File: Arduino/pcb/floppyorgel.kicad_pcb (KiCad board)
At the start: 2 copper layers, 50 x 50 mm, 13 parts, among them J1 Floppy-Bus, J2 Floppy-Bus, J3 FTDI, J4 Buck Converter 5V, J5 MAX485 Socket, J6 Buck Converter 12V, J7 IBM_PC_IDC_Connector, J8 Power Select, J9 Floppy Power, SW1 Bus Address Select, SW2 Reset Button, U1 ATMEGA328P-AU

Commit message: pcb: update
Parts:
- removed REF**: Floppy_Power, Pin_Headers:Pin_Header_Straight_1x04_Pitch2.54mm
- added U2: 74HC595, SMD_Packages:SO-16-N, F.Cu at (108.0, 113.0)
- added U3: 74LS166, SMD_Packages:SO-16-N, F.Cu at (142.0, 113.0)
- added Y1: 20 Mhz Crystal, Crystals:Crystal_HC49-4H_Vertical, F.Cu at (115.6, 139.7)
- moved J2 10.8 mm to (142.2, 133.3), turned to 180 degrees
- moved J8 1.43 mm to (104.0, 138.4)
- moved J3 1.05 mm to (104.0, 146.1)
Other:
- board text added: "5V GND GND 12V"

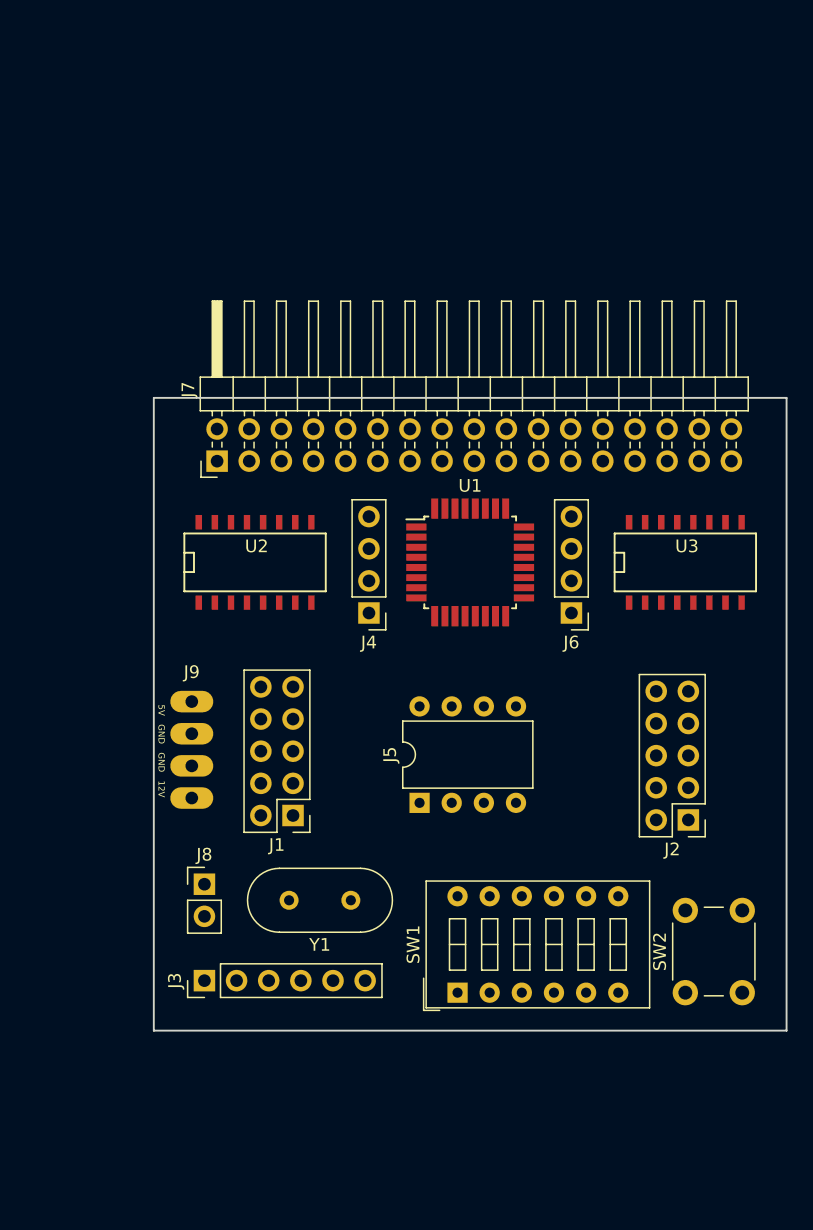
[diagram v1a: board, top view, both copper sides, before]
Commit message: pcb: add I2C eeprom
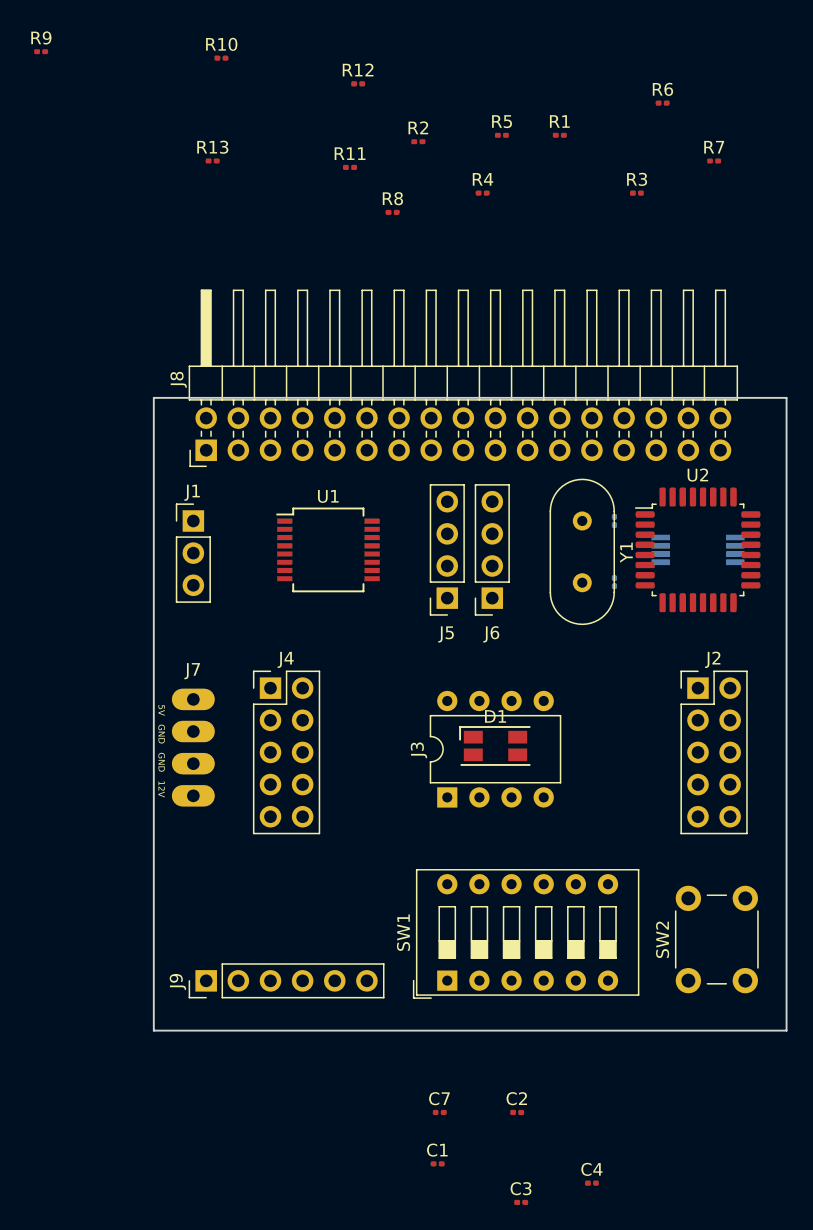
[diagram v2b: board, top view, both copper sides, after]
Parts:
- added C1: 100nF, Capacitor_SMD:C_0201_0603Metric, F.Cu at (122.4, 160.5)
- added C2: 100nF, Capacitor_SMD:C_0201_0603Metric, F.Cu at (128.7, 156.5)
- added C3: 100nF, Capacitor_SMD:C_0201_0603Metric, F.Cu at (129.0, 163.6)
- added C4: 100nF, Capacitor_SMD:C_0201_0603Metric, F.Cu at (134.6, 162.1)
- added C5: 22pF, Capacitor_SMD:C_0201_0603Metric, B.Cu at (136.4, 114.6)
- added C6: 22pF, Capacitor_SMD:C_0201_0603Metric, B.Cu at (136.4, 109.7)
- added C7: 100nF, Capacitor_SMD:C_0201_0603Metric, F.Cu at (122.6, 156.5)
- added D1: WS2812B, LED_SMD:LED_RGB_1210, F.Cu at (127.0, 127.5)
- added R1: 4K7, Capacitor_SMD:C_0201_0603Metric, F.Cu at (132.1, 79.2)
- added R10: 4K7, Capacitor_SMD:C_0201_0603Metric, F.Cu at (105.3, 73.2)
- added R11: 4K7, Capacitor_SMD:C_0201_0603Metric, F.Cu at (115.5, 81.8)
- added R12: 4K7, Capacitor_SMD:C_0201_0603Metric, F.Cu at (116.1, 75.2)
- added R13: 4K7, Capacitor_SMD:C_0201_0603Metric, F.Cu at (104.6, 81.3)
- added R2: 4K7, Capacitor_SMD:C_0201_0603Metric, F.Cu at (120.9, 79.8)
- added R3: 4K7, Capacitor_SMD:C_0201_0603Metric, F.Cu at (138.2, 83.8)
- added R4: 4K7, Capacitor_SMD:C_0201_0603Metric, F.Cu at (126.0, 83.8)
- added R5: 4K7, Capacitor_SMD:C_0201_0603Metric, F.Cu at (127.5, 79.2)
- added R6: 4K7, Capacitor_SMD:C_0201_0603Metric, F.Cu at (140.2, 76.7)
- added R7: 100R, Capacitor_SMD:C_0201_0603Metric, F.Cu at (144.3, 81.3)
- added R8: 100R, Capacitor_SMD:C_0201_0603Metric, F.Cu at (118.9, 85.3)
- added R9: 10K, Capacitor_SMD:C_0201_0603Metric, F.Cu at (91.1, 72.6)
- J1: value Floppy-Bus -> VCC_Power_Select; footprint Pin_Headers:Pin_Header_Straight_2x05_Pitch2.54mm -> Connector_PinHeader_2.54mm:PinHeader_1x03_P2.54mm_Vertical
- J2: footprint Pin_Headers:Pin_Header_Straight_2x05_Pitch2.54mm -> shrouded:Shrouded_Header_2x05_Pitch2.54mm
- J3: value FTDI -> MAX485 Socket; footprint Pin_Headers:Pin_Header_Straight_1x06_Pitch2.54mm -> Package_DIP:DIP-8_W7.62mm
- J4: value Buck Converter 5V -> Floppy-Bus; footprint Pin_Headers:Pin_Header_Straight_1x04_Pitch2.54mm -> shrouded:Shrouded_Header_2x05_Pitch2.54mm
- J5: value MAX485 Socket -> Buck-Converter-5V; footprint Housings_DIP:DIP-8_W7.62mm -> Connector_PinSocket_2.54mm:PinSocket_1x04_P2.54mm_Vertical
- J6: value Buck Converter 12V -> Buck-Converter-12V; footprint Pin_Headers:Pin_Header_Straight_1x04_Pitch2.54mm -> Connector_PinSocket_2.54mm:PinSocket_1x04_P2.54mm_Vertical
- J7: value IBM_PC_IDC_Connector -> Floppy-Power; footprint Pin_Headers:Pin_Header_Angled_2x17_Pitch2.54mm -> floppy_power:Floppy_Power_1x04_Pitch2.54mm
- J8: value Power Select -> IBM_PC_Floppy_IDC; footprint Pin_Headers:Pin_Header_Straight_1x02_Pitch2.54mm -> Connector_PinHeader_2.54mm:PinHeader_2x17_P2.54mm_Horizontal
- J9: value Floppy Power -> FTDI; footprint floppy_power:Pin_Header_Straight_1x04_Pitch2.54mm -> Connector_PinHeader_2.54mm:PinHeader_1x06_P2.54mm_Vertical
- SW1: footprint Buttons_Switches_THT:SW_DIP_x6_W7.62mm_Slide -> Button_Switch_THT:SW_DIP_SPSTx06_Slide_9.78x17.42mm_W7.62mm_P2.54mm
- SW2: footprint Buttons_Switches_THT:SW_PUSH_6mm -> Button_Switch_THT:SW_PUSH_6mm
- U1: value ATMEGA328P-AU -> 4021; footprint Housings_QFP:TQFP-32_7x7mm_Pitch0.8mm -> Package_SO:SSOP-16_5.3x6.2mm_P0.65mm
- U2: value 74HC595 -> ATMEGA328P-AU; footprint SMD_Packages:SO-16-N -> Package_QFP:LQFP-32_7x7mm_P0.8mm
- U3: value 74LS166 -> 24LC64; footprint SMD_Packages:SO-16-N -> Package_SO:TSSOP-8_4.4x3mm_P0.65mm; moved to B.Cu
- Y1: footprint Crystals:Crystal_HC49-4H_Vertical -> Crystal:Crystal_HC49-4H_Vertical
- moved Y1 35.1 mm to (133.9, 109.7), turned to 270 degrees
- moved U2 35.0 mm to (143.0, 112.0)
- moved J8 34.3 mm to (104.1, 104.1), turned to 90 degrees
- moved J1 24.6 mm to (103.1, 109.7), turned to 0 degrees
- moved J3 24.0 mm to (123.2, 131.6)
- moved J9 22.1 mm to (104.1, 146.1), turned to 90 degrees
- moved J7 18.9 mm to (103.1, 123.8), turned to 0 degrees
- moved J5 16.3 mm to (123.2, 115.8), turned to 180 degrees
- moved U1 11.3 mm to (113.8, 112.0)
- moved J2 10.4 mm to (143.0, 122.9), turned to 0 degrees
- moved J4 9.79 mm to (109.2, 122.9), turned to 0 degrees
- moved J6 6.36 mm to (126.7, 115.8)
- moved U3 1.41 mm to (143.0, 112.0), turned to 180 degrees
- moved SW1 1.25 mm to (123.2, 146.1)
- moved SW2 0.98 mm to (142.2, 146.1)
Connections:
- J1 pad 1: Net-(J1-Pad1) -> /5V_ISP
- J1 pad 2: Net-(J1-Pad2) -> VCC
- J1 pad 3: Net-(J1-Pad3) -> /5V_BUS
- J2 pad 1: Net-(J2-Pad1) -> /Bus/BUS_POWER
- J2 pad 3: Net-(J2-Pad3) -> GND
- J2 pad 5: Net-(J2-Pad5) -> (no net)
- J2 pad 6: Net-(J2-Pad6) -> (no net)
- J3 pad 1: Net-(J3-Pad1) -> /MCU/RX
- J3 pad 2: Net-(J3-Pad2) -> GND
- J3 pad 3: Net-(J3-Pad3) -> GND
- J3 pad 4: Net-(J3-Pad4) -> /Bus/RX
- J3 pad 5: Net-(J3-Pad5) -> GND
- J3 pad 6: Net-(J3-Pad6) -> Net-(J2-Pad7)
- J4 pad 1: Net-(J4-Pad1) -> Net-(J2-Pad2)
- J4 pad 2: Net-(J4-Pad2) -> (no net)
- J4 pad 3: Net-(J4-Pad3) -> Net-(J2-Pad4)
- J4 pad 4: Net-(J4-Pad4) -> (no net)
- J5 pad 1: Net-(J5-Pad1) -> /Bus/BUS_POWER
- J5 pad 2: Net-(J5-Pad2) -> /Bus/BUS_POWER
- J5 pad 3: Net-(J5-Pad3) -> GND
- J5 pad 4: Net-(J5-Pad4) -> /5V_BUS
- J6 pad 1: Net-(J6-Pad1) -> /Bus/BUS_POWER
- J6 pad 2: Net-(J6-Pad2) -> /Bus/BUS_POWER
- J6 pad 3: Net-(J6-Pad3) -> GND
- J6 pad 4: Net-(J6-Pad4) -> /Floppy/12V_BUS
- J7 pad 1: Net-(J7-Pad1) -> /5V_BUS
- J7 pad 2: Net-(J7-Pad2) -> GND
- J7 pad 3: Net-(J7-Pad3) -> GND
- J7 pad 4: Net-(J7-Pad4) -> /Floppy/12V_BUS
- J8 pad 1: Net-(J8-Pad1) -> GND
- J8 pad 2: Net-(J8-Pad2) -> (no net)
- J9 pad 1: Net-(J9-Pad1) -> GND
- J9 pad 2: Net-(J9-Pad2) -> (no net)
- J9 pad 3: Net-(J9-Pad3) -> /5V_ISP
- SW1 pad 1: Net-(SW1-Pad1) -> VCC
- SW1 pad 10: Net-(SW1-Pad10) -> Net-(R4-Pad1)
- SW1 pad 11: Net-(SW1-Pad11) -> Net-(R5-Pad1)
- SW1 pad 12: Net-(SW1-Pad12) -> Net-(R6-Pad1)
- SW1 pad 2: Net-(SW1-Pad2) -> VCC
- SW1 pad 3: Net-(SW1-Pad3) -> VCC
- SW1 pad 4: Net-(SW1-Pad4) -> VCC
- SW1 pad 5: Net-(SW1-Pad5) -> VCC
- SW1 pad 6: Net-(SW1-Pad6) -> VCC
- SW1 pad 7: Net-(SW1-Pad7) -> Net-(R1-Pad1)
- SW1 pad 8: Net-(SW1-Pad8) -> Net-(R2-Pad1)
- SW1 pad 9: Net-(SW1-Pad9) -> Net-(R3-Pad1)
- SW2 pad 1: Net-(SW2-Pad1) -> Net-(C4-Pad1)
- U1 pad 1: Net-(U1-Pad1) -> GND
- U1 pad 10: Net-(U1-Pad10) -> /Floppy/SCK
- U1 pad 11: Net-(U1-Pad11) -> GND
- U1 pad 12: Net-(U1-Pad12) -> (no net)
- U1 pad 13: Net-(U1-Pad13) -> Net-(R2-Pad1)
- U1 pad 14: Net-(U1-Pad14) -> Net-(R1-Pad1)
- U1 pad 15: Net-(U1-Pad15) -> GND
- U1 pad 16: Net-(U1-Pad16) -> VCC
- U1 pad 2: Net-(U1-Pad2) -> (no net)
- U1 pad 3: Net-(U1-Pad3) -> /Floppy/MISO
- U1 pad 4: Net-(U1-Pad4) -> Net-(R3-Pad1)
- U1 pad 5: Net-(U1-Pad5) -> Net-(R4-Pad1)
- U1 pad 6: Net-(U1-Pad6) -> Net-(R5-Pad1)
- U1 pad 7: Net-(U1-Pad7) -> Net-(R6-Pad1)
- U1 pad 8: Net-(U1-Pad8) -> GND
- U1 pad 9: Net-(U1-Pad9) -> /Floppy/LATCH_ADDR
- U2 pad 1: Net-(U2-Pad1) -> (no net)
- U2 pad 10: Net-(U2-Pad10) -> (no net)
- U2 pad 11: Net-(U2-Pad11) -> (no net)
- U2 pad 12: Net-(U2-Pad12) -> /Floppy/DRIVE_SELECT
- U2 pad 13: Net-(U2-Pad13) -> /Floppy/DIRECTION
- U2 pad 14: Net-(U2-Pad14) -> /Floppy/STEP
- U2 pad 15: Net-(U2-Pad15) -> (no net)
- U2 pad 16: VCC -> /Floppy/MISO
- U2 pad 2: Net-(U2-Pad2) -> (no net)
- U2 pad 3: Net-(U2-Pad3) -> GND
- U2 pad 4: Net-(U2-Pad4) -> VCC
- U2 pad 5: Net-(U2-Pad5) -> GND
- U2 pad 6: Net-(U2-Pad6) -> VCC
- U2 pad 7: Net-(U2-Pad7) -> Net-(C5-Pad2)
- U2 pad 8: GND -> Net-(C6-Pad1)
- U2 pad 9: Net-(U2-Pad9) -> (no net)
- U3 pad 1: Net-(U3-Pad1) -> GND
- U3 pad 2: Net-(U3-Pad2) -> GND
- U3 pad 3: Net-(U3-Pad3) -> GND
- U3 pad 4: Net-(U3-Pad4) -> GND
- U3 pad 5: Net-(U3-Pad5) -> /MCU/SDA
- U3 pad 6: Net-(U3-Pad6) -> /MCU/SCL
- U3 pad 7: Net-(U3-Pad7) -> GND
- U3 pad 8: GND -> VCC
- Y1 pad 1: Net-(Y1-Pad1) -> Net-(C6-Pad1)
- Y1 pad 2: Net-(Y1-Pad2) -> Net-(C5-Pad2)

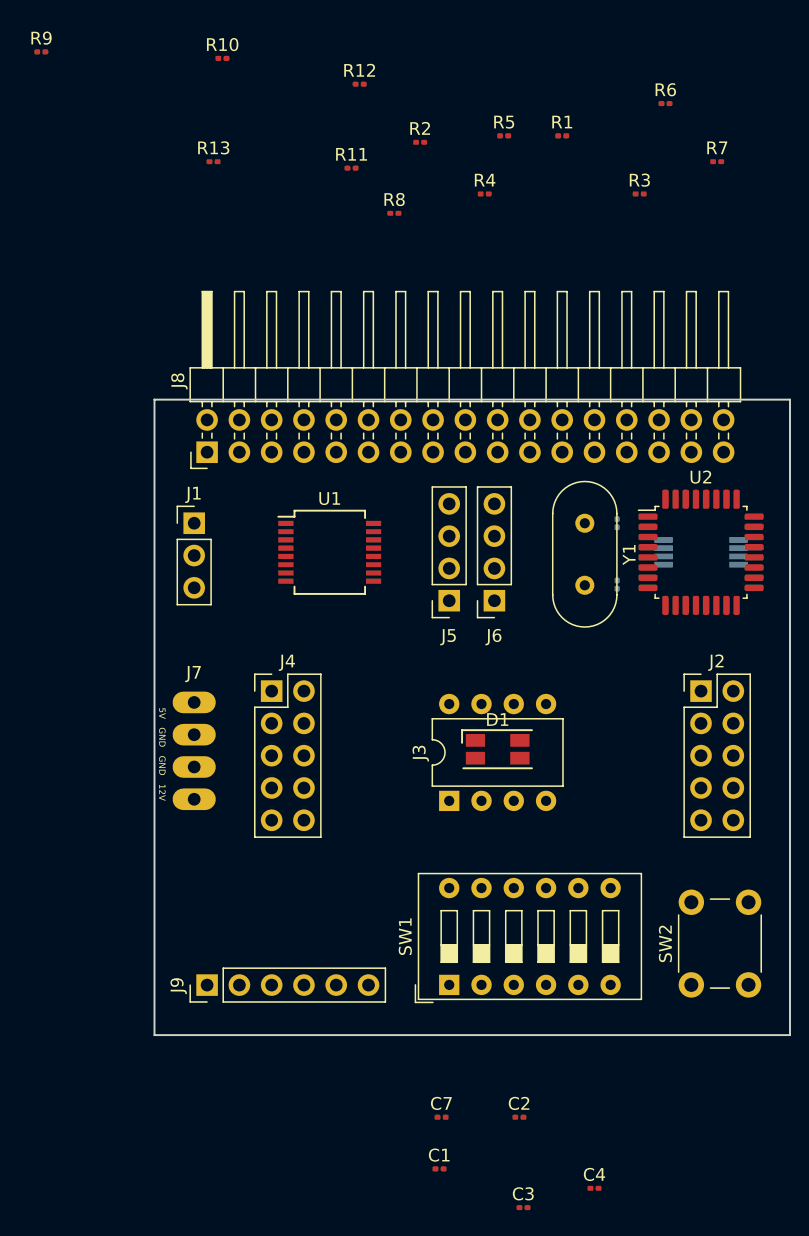
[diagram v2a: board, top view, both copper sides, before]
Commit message: pcb: finished part placement
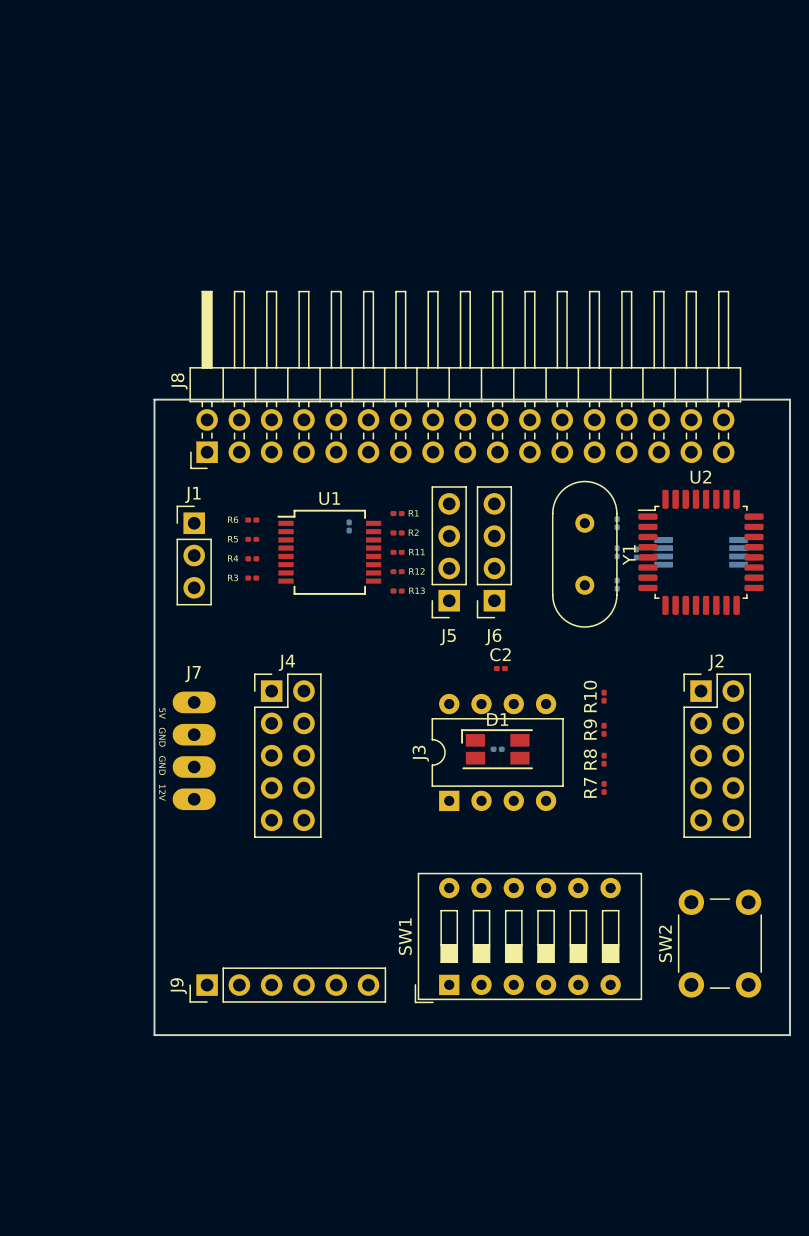
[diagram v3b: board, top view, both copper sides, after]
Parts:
- C1, C3, C4, C7: moved to B.Cu
- moved R9 69.3 mm to (135.4, 126.0), turned to 90 degrees
- moved R10 58.5 mm to (135.4, 123.4), turned to 90 degrees
- moved C1 50.5 mm to (136.4, 112.0), turned to 270 degrees
- moved R7 50.1 mm to (135.4, 130.6), turned to 90 degrees
- moved C4 50.1 mm to (137.9, 112.1), turned to 270 degrees
- moved C7 47.0 mm to (115.3, 110.0), turned to 270 degrees
- moved R6 46.2 mm to (107.7, 109.5)
- moved R8 46.1 mm to (135.4, 128.3), turned to 90 degrees
- moved R3 42.9 mm to (107.7, 114.0)
- moved R12 38.5 mm to (119.1, 113.5)
- moved R5 37.4 mm to (107.7, 111.0), turned to 180 degrees
- moved R13 36.8 mm to (119.1, 115.1)
- moved C3 36.1 mm to (127.0, 127.5)
- moved C2 35.3 mm to (127.3, 121.2)
- moved R4 34.0 mm to (107.7, 112.5)
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
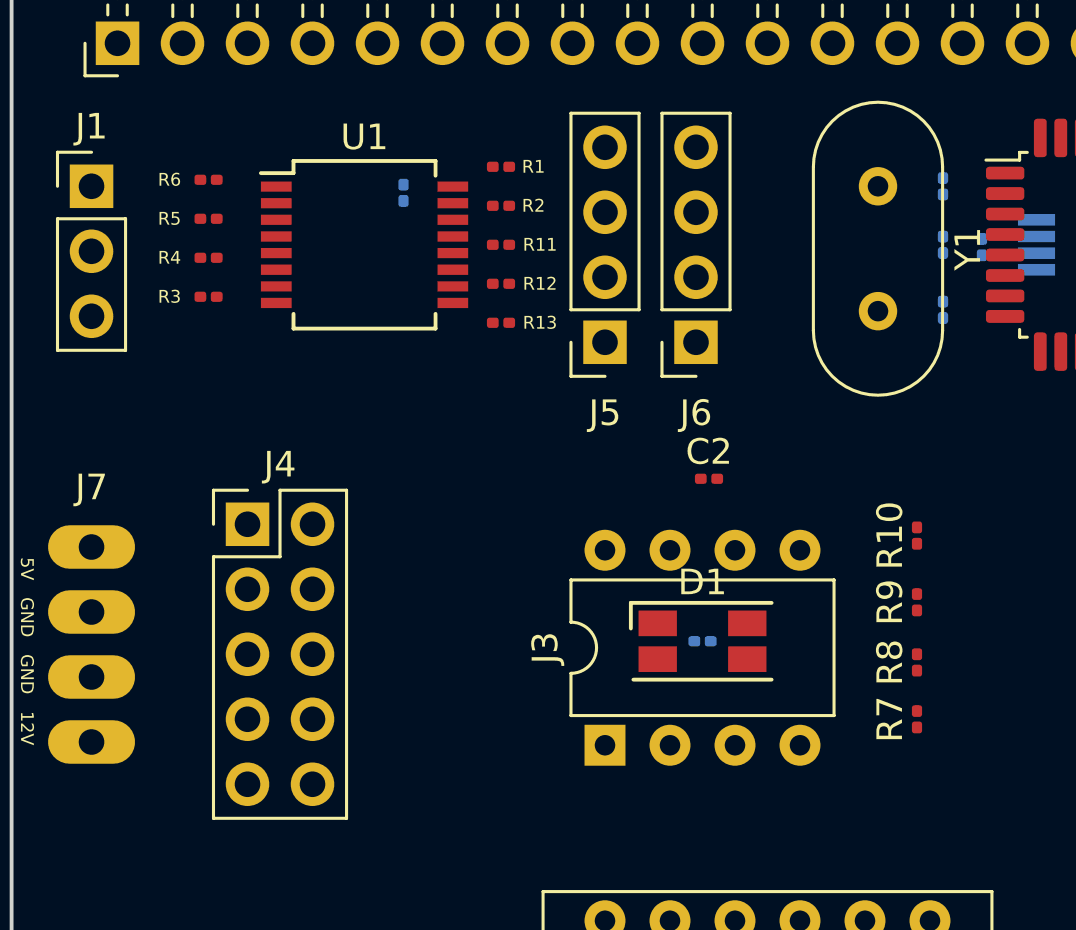
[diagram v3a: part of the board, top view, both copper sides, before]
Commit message: pcb: add SOIC-8 socket footprint + 3D model
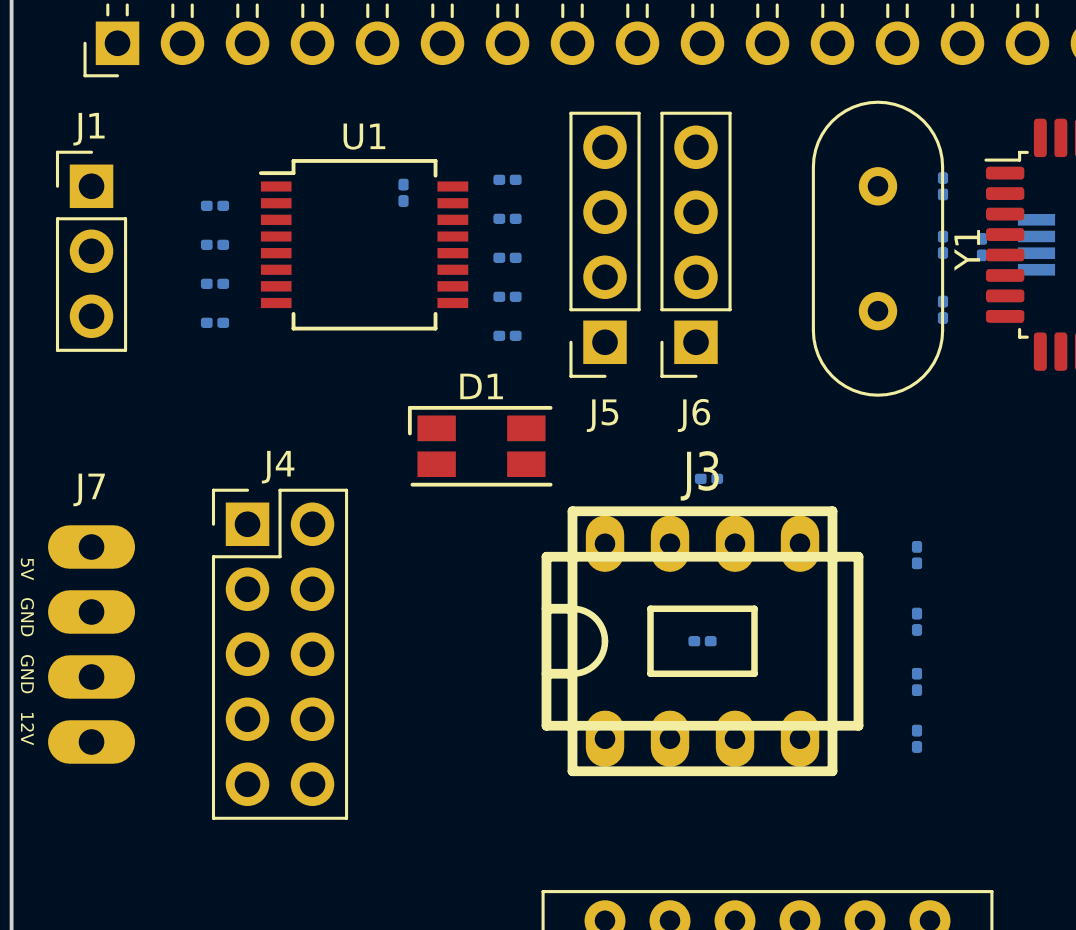
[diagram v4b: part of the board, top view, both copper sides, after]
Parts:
- C2, R1, R10, R11, R12, R13, R2, R3, R4, R5, R6, R7, R8, R9: moved to B.Cu
- J3: footprint Package_DIP:DIP-8_W7.62mm -> dil:dil_8-300_socket
- moved D1 11.5 mm to (118.4, 119.9)
- moved R1 6.61 mm to (119.4, 115.6)
- moved R13 5.59 mm to (119.4, 109.5)
- moved R6 5.59 mm to (108.0, 115.1)
- moved J3 5.57 mm to (127.0, 127.5), turned to 0 degrees
- moved R3 3.57 mm to (108.0, 110.5)
- moved R2 3.57 mm to (119.4, 114.0)
- moved R5 2.55 mm to (108.0, 113.5)
- moved R12 2.55 mm to (119.4, 111.0)
- moved R10 0.76 mm to (135.4, 124.1), turned to 270 degrees
- moved R7 0.76 mm to (135.4, 131.3), turned to 270 degrees
- moved R8 0.76 mm to (135.4, 129.1), turned to 270 degrees
- moved R9 0.76 mm to (135.4, 126.7), turned to 270 degrees
- moved R4 0.57 mm to (108.0, 112.0)
- moved R11 0.57 mm to (119.4, 112.5)
